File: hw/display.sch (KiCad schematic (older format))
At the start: 16 parts, among them J1 IDC_02X03, J2 SWD_01X04, Q1 Q_NMOS_DGS, U1 RC1602B, U2 STM32F042F6Px, U3 74AHC1G08

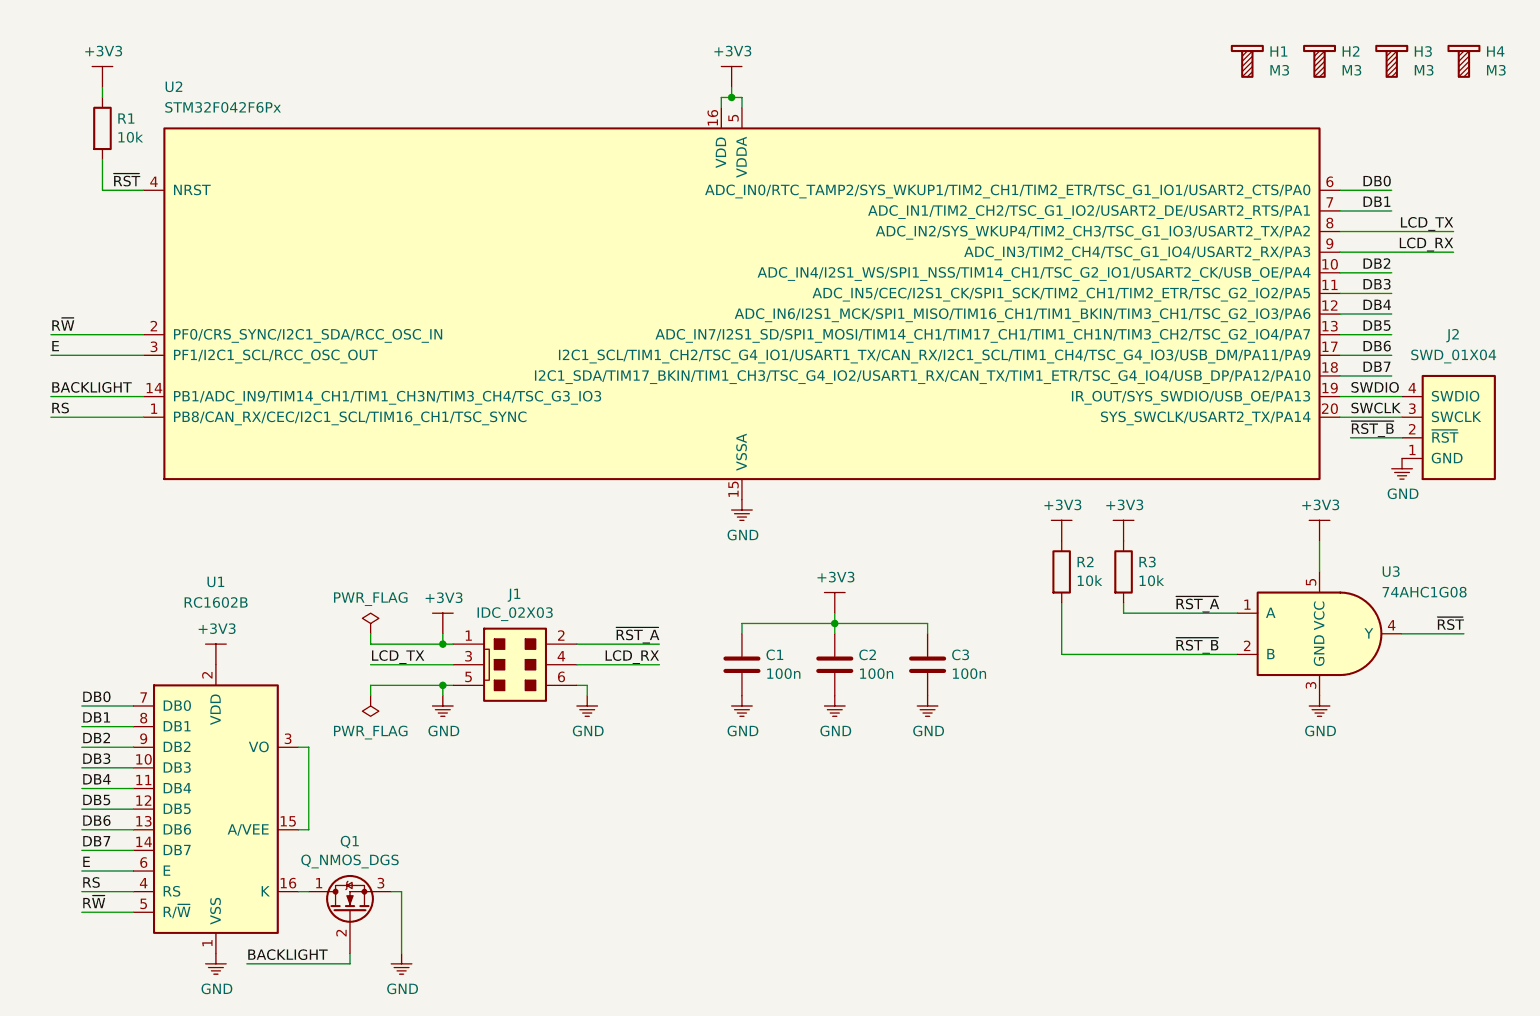
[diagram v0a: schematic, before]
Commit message: updated schematic universaled display and removed rst b signal
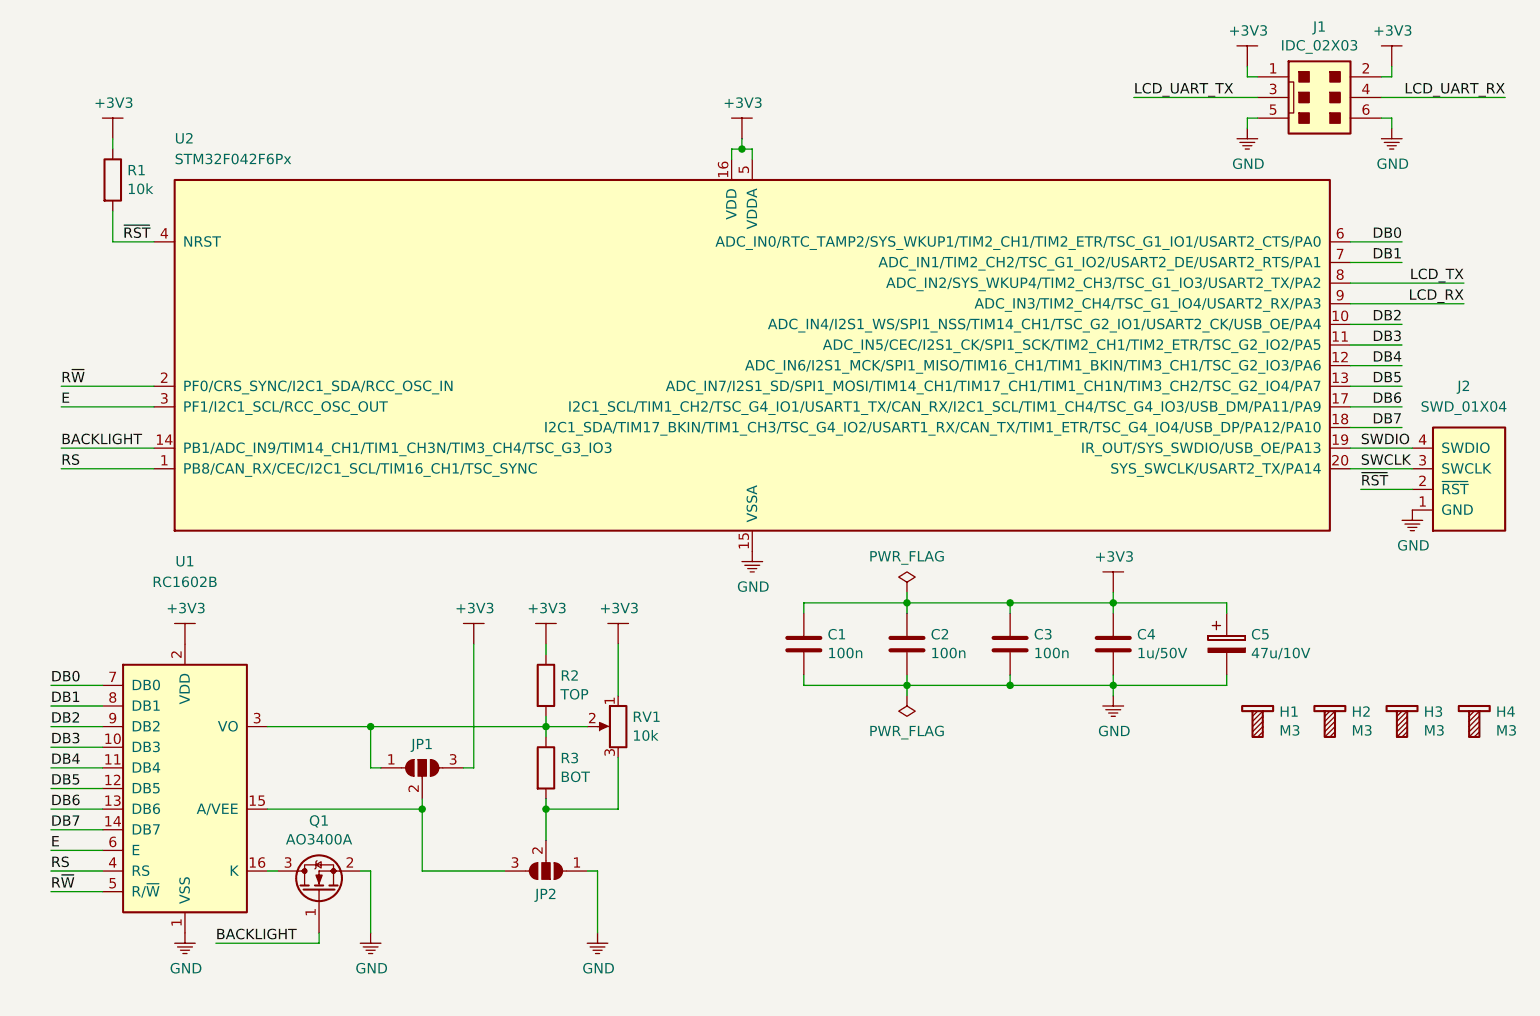
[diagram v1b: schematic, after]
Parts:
- removed Q1: Q_NMOS_DGS, symbol Device:Q_NMOS_DGS
- removed U3: 74AHC1G08, Package_TO_SOT_SMD:SOT-23-5, symbol KLIB_Logic:74AHC1G08
- added C4: 1u/50V, Capacitor_SMD:C_0805_2012Metric, symbol Device:C
- added C5: 47u/10V, Capacitor_Tantalum_SMD:CP_EIA-3528-21_Kemet-B, symbol Device:CP
- added JP1, JP2: SolderJumper_3_Open, Jumper:SolderJumper-3_P1.3mm_Open_RoundedPad1.0x1.5mm_NumberLabels, symbol Jumper:SolderJumper_3_Open
- added Q1: AO3400A, Package_TO_SOT_SMD:SOT-23, symbol Device:Q_NMOS_GSD
- added RV1: 10k, Potentiometer_THT:Potentiometer_ACP_CA9-H3,8_Horizontal, symbol Device:POT
- C1, C2, C3: footprint (none) -> Capacitor_SMD:C_0805_2012Metric
- R1: footprint (none) -> Resistor_SMD:R_0805_2012Metric
- R2: value 10k -> TOP; footprint (none) -> Resistor_SMD:R_0805_2012Metric
- R3: value 10k -> BOT; footprint (none) -> Resistor_SMD:R_0805_2012Metric
- U1: footprint Display:RC1602A -> Display:WC1602A
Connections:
- net +3V3: now also J1.2, C4.1, C5.1, JP1.3 (B), RV1.1; no longer R3.1
- net BACKLIGHT: now also Q1.1 (G)
- net GND: now also C4.2, C5.2, JP2.1 (A), Q1.2 (S)
- net LCD_RX: no longer J1.4
- net LCD_TX: no longer J1.3
- net ~RST: now also J2.2 (~RST)
- net at U1.15 (A/VEE): now also JP1.2 (C), JP2.3 (B); no longer U1.3 (VO)
- net at U1.16 (K): now also Q1.3 (D)
- net ~RST_A: no longer names the net of R3.2
- net ~RST_A: now also JP2.2 (C), RV1.3; no longer J1.2
- net ~RST_B: no longer names the net of R2.2
- net ~RST_B: now also R3.1, U1.3 (VO), JP1.1 (A), RV1.2; no longer J2.2 (~RST)
- new net LCD_UART_RX: J1.4
- new net LCD_UART_TX: J1.3
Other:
- moved on the sheet: C1, C2, C3, H1, H2, H3, H4, J1, J2, R1, U1, U2

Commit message: placement components to pcb
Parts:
- J1: footprint Connectors:IDC_Header_Straight_6pins -> Connector_IDC:IDC-Header_2x03_P2.54mm_Vertical
- U1: footprint Display:WC1602A -> KLIB_Display:RC1602B
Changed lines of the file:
@@
-$EndComp
-$Comp
-L KLIB_Display:RC1602B U1
-U 1 1 5ABEE4F3
-P 1250 4250
-F 0 "U1" H 1250 5350 50  0000 C CNN
-F 1 "RC1602B" H 1250 5250 50  0000 C CNN
-F 2 "Display:WC1602A" H 1600 3550 50  0001 C CNN
-F 3 "https://www.tme.eu/cz/Document/80bdbedf6bf0a19df5cdc5be2a2c033c/RC1602B-LLB-JWVE.pdf" H 1350 4150 50  0001 C CNN
-	1    1250 4250
-	1    0    0    -1
 $EndComp
 $Comp
@@
 R~W
 $Comp
-L KLIB_Connector_IDC:IDC_02X03 J1
-U 1 1 5AD5A855
-P 6750 900
-F 0 "J1" H 6750 1242 50  0000 C CNN
-F 1 "IDC_02X03" H 6750 1151 50  0000 C CNN
-F 2 "Connectors:IDC_Header_Straight_6pins" V 7300 900 50  0001 C CNN
-F 3 "~" V 7250 900 50  0001 C CNN
-	1    6750 900
-	1    0    0    -1
-$EndComp
-$Comp
 L KLIB_Power:GND #PWR014
 U 1 1 5AD5A906
@@
 	0    -1   -1   0
 $EndComp
+$Comp
+L KLIB_Connector_IDC:IDC_02X03 J1
+U 1 1 5AF01E77
+P 6750 900
+F 0 "J1" H 6750 1242 50  0000 C CNN
+F 1 "IDC_02X03" H 6750 1151 50  0000 C CNN
+F 2 "Connector_IDC:IDC-Header_2x03_P2.54mm_Vertical" V 7300 900 50  0001 C CNN
+F 3 "~" V 7250 900 50  0001 C CNN
+	1    6750 900
+	1    0    0    -1
+$EndComp
+$Comp
+L KLIB_Display:RC1602B U1
+U 1 1 5AD955BE
+P 1250 4250
+F 0 "U1" H 1500 5050 50  0000 L CNN
+F 1 "RC1602B" H 1500 4950 50  0000 L CNN
+F 2 "KLIB_Display:RC1602B" H 1300 3550 50  0001 L CNN
+F 3 "https://www.tme.eu/cz/Document/80bdbedf6bf0a19df5cdc5be2a2c033c/RC1602B-LLB-JWVE.pdf" H 1350 4050 50  0001 C CNN
+	1    1250 4250
+	1    0    0    -1
+$EndComp
 $EndSCHEMATC

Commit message: updated pcb
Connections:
- net LCD_RX is gone; now on net LCD_UART_RX: U2.9 (ADC_IN3/TIM2_CH4/TSC_G1_IO4/USART2_RX/PA3)
- net LCD_TX is gone; now on net LCD_UART_TX: U2.8 (ADC_IN2/SYS_WKUP4/TIM2_CH3/TSC_G1_IO3/USART2_TX/PA2)
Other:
- moved on the sheet: Q1
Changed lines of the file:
@@
 L KLIB_Power:GND #PWR04
 U 1 1 5ABEEAEB
-P 2150 4950
-F 0 "#PWR04" H 2150 4750 50  0001 C CNN
-F 1 "GND" H 2155 4777 50  0000 C CNN
-F 2 "" H 2150 4950 50  0001 C CNN
-F 3 "" H 2150 4950 50  0001 C CNN
-	1    2150 4950
+P 2300 4950
+F 0 "#PWR04" H 2300 4750 50  0001 C CNN
+F 1 "GND" H 2305 4777 50  0000 C CNN
+F 2 "" H 2300 4950 50  0001 C CNN
+F 3 "" H 2300 4950 50  0001 C CNN
+	1    2300 4950
 	1    0    0    -1
 $EndComp
@@
 $EndComp
 Wire Wire Line
-	2150 4950 2150 4650
-Wire Wire Line
-	2150 4650 2100 4650
-Wire Wire Line
-	1700 4650 1650 4650
+	2300 4950 2300 4650
+Wire Wire Line
+	2300 4650 2250 4650
+Wire Wire Line
+	1850 4650 1750 4650
 $Comp
 L MCU_ST_STM32:STM32F042F6Px U2
@@
 	6900 1900 7450 1900
 Text Label 7450 1900 2    50   ~ 0
-LCD_RX
+LCD_UART_RX
 Wire Wire Line
 	6900 1800 7450 1800
 Text Label 7450 1800 2    50   ~ 0
-LCD_TX
-Wire Wire Line
-	1400 5000 1900 5000
-Wire Wire Line
-	1900 5000 1900 4950
-Text Label 1400 5000 0    50   ~ 0
+LCD_UART_TX
+Wire Wire Line
+	1550 5000 2050 5000
+Wire Wire Line
+	2050 5000 2050 4950
+Text Label 1550 5000 0    50   ~ 0
 BACKLIGHT
 Text Label 650  2600 0    50   ~ 0
@@
 	650  2600 1100 2600
 Wire Wire Line
-	1100 2400 650  2400
+	1100 2400 1000 2400
 Wire Wire Line
 	1100 2700 650  2700
@@
 Text Label 650  2700 0    50   ~ 0
 RS
-Wire Wire Line
-	1100 2300 650  2300
 Text Label 650  2300 0    50   ~ 0
 R~W
@@
 L Device:Q_NMOS_GSD Q1
 U 1 1 5AF01164
-P 1900 4750
-F 0 "Q1" V 2243 4750 50  0000 C CNN
-F 1 "AO3400A" V 2152 4750 50  0000 C CNN
-F 2 "Package_TO_SOT_SMD:SOT-23" H 2100 4850 50  0001 C CNN
-F 3 "https://www.tme.eu/cz/details/ao3400a/tranzistory-s-kanalem-n-smd/alpha-omega-semiconductor/" H 1900 4750 50  0001 C CNN
-	1    1900 4750
+P 2050 4750
+F 0 "Q1" V 2393 4750 50  0000 C CNN
+F 1 "AO3400A" V 2302 4750 50  0000 C CNN
+F 2 "Package_TO_SOT_SMD:SOT-23" H 2250 4850 50  0001 C CNN
+F 3 "https://www.tme.eu/cz/details/ao3400a/tranzistory-s-kanalem-n-smd/alpha-omega-semiconductor/" H 2050 4750 50  0001 C CNN
+	1    2050 4750
 	0    -1   -1   0
 $EndComp
@@
 	1    0    0    -1
 $EndComp
+$Comp
+L KLIB_Power:PWR_FLAG #FLG0101
+U 1 1 5AD9621D
+P 2150 3900
+F 0 "#FLG0101" H 2150 3975 50  0001 C CNN
+F 1 "PWR_FLAG" H 2150 4074 50  0000 C CNN
+F 2 "" H 2150 3900 50  0001 C CNN
+F 3 "" H 2150 3900 50  0001 C CNN
+	1    2150 3900
+	1    0    0    -1
+$EndComp
+Wire Wire Line
+	2150 3900 2150 3950
+$Comp
+L KLIB_Power:PWR_FLAG #FLG0102
+U 1 1 5AD9892B
+P 1750 3900
+F 0 "#FLG0102" H 1750 3975 50  0001 C CNN
+F 1 "PWR_FLAG" H 1750 4074 50  0000 C CNN
+F 2 "" H 1750 3900 50  0001 C CNN
+F 3 "" H 1750 3900 50  0001 C CNN
+	1    1750 3900
+	1    0    0    -1
+$EndComp
+Wire Wire Line
+	1750 3900 1750 4650
+Connection ~ 1750 4650
+Wire Wire Line
+	1750 4650 1650 4650
+$Comp
+L KLIB_Power:PWR_FLAG #FLG0103
+U 1 1 5ADA0448
+P 1000 2000
+F 0 "#FLG0103" H 1000 2075 50  0001 C CNN
+F 1 "PWR_FLAG" V 1000 2128 50  0000 L CNN
+F 2 "" H 1000 2000 50  0001 C CNN
+F 3 "" H 1000 2000 50  0001 C CNN
+	1    1000 2000
+	0    -1   -1   0
+$EndComp
+$Comp
+L KLIB_Power:PWR_FLAG #FLG0104
+U 1 1 5ADA0599
+P 1000 1900
+F 0 "#FLG0104" H 1000 1975 50  0001 C CNN
+F 1 "PWR_FLAG" V 1000 2028 50  0000 L CNN
+F 2 "" H 1000 1900 50  0001 C CNN
+F 3 "" H 1000 1900 50  0001 C CNN
+	1    1000 1900
+	0    -1   -1   0
+$EndComp
+Wire Wire Line
+	1000 1900 1100 1900
+Wire Wire Line
+	1100 1900 1100 2300
+Connection ~ 1100 2300
+Wire Wire Line
+	650  2300 1100 2300
+Wire Wire Line
+	1000 2000 1000 2400
+Connection ~ 1000 2400
+Wire Wire Line
+	1000 2400 650  2400
 $EndSCHEMATC
